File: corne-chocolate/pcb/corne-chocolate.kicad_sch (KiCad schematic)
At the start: 59 parts, among them J1 MJ-4PP-9, J2 OLED, P1 i2c-pin, P2 i2c-pin, SW1 SW_PUSH, SW10 SW_PUSH, SW11 SW_PUSH, SW12 SW_PUSH, SW13 SW_PUSH, SW14 SW_PUSH, SW15 SW_PUSH, SW16 SW_PUSH, SW17 SW_PUSH, SW18 SW_PUSH, SW19 SW_PUSH, SW2 SW_PUSH, SW20 SW_PUSH, SW21 SW_PUSH, SW3 SW_PUSH, SW4 SW_PUSH, SW5 SW_PUSH, SW6 SW_PUSH, SW7 SW_PUSH, SW8 SW_PUSH, SW9 SW_PUSH, U1 ProMicro

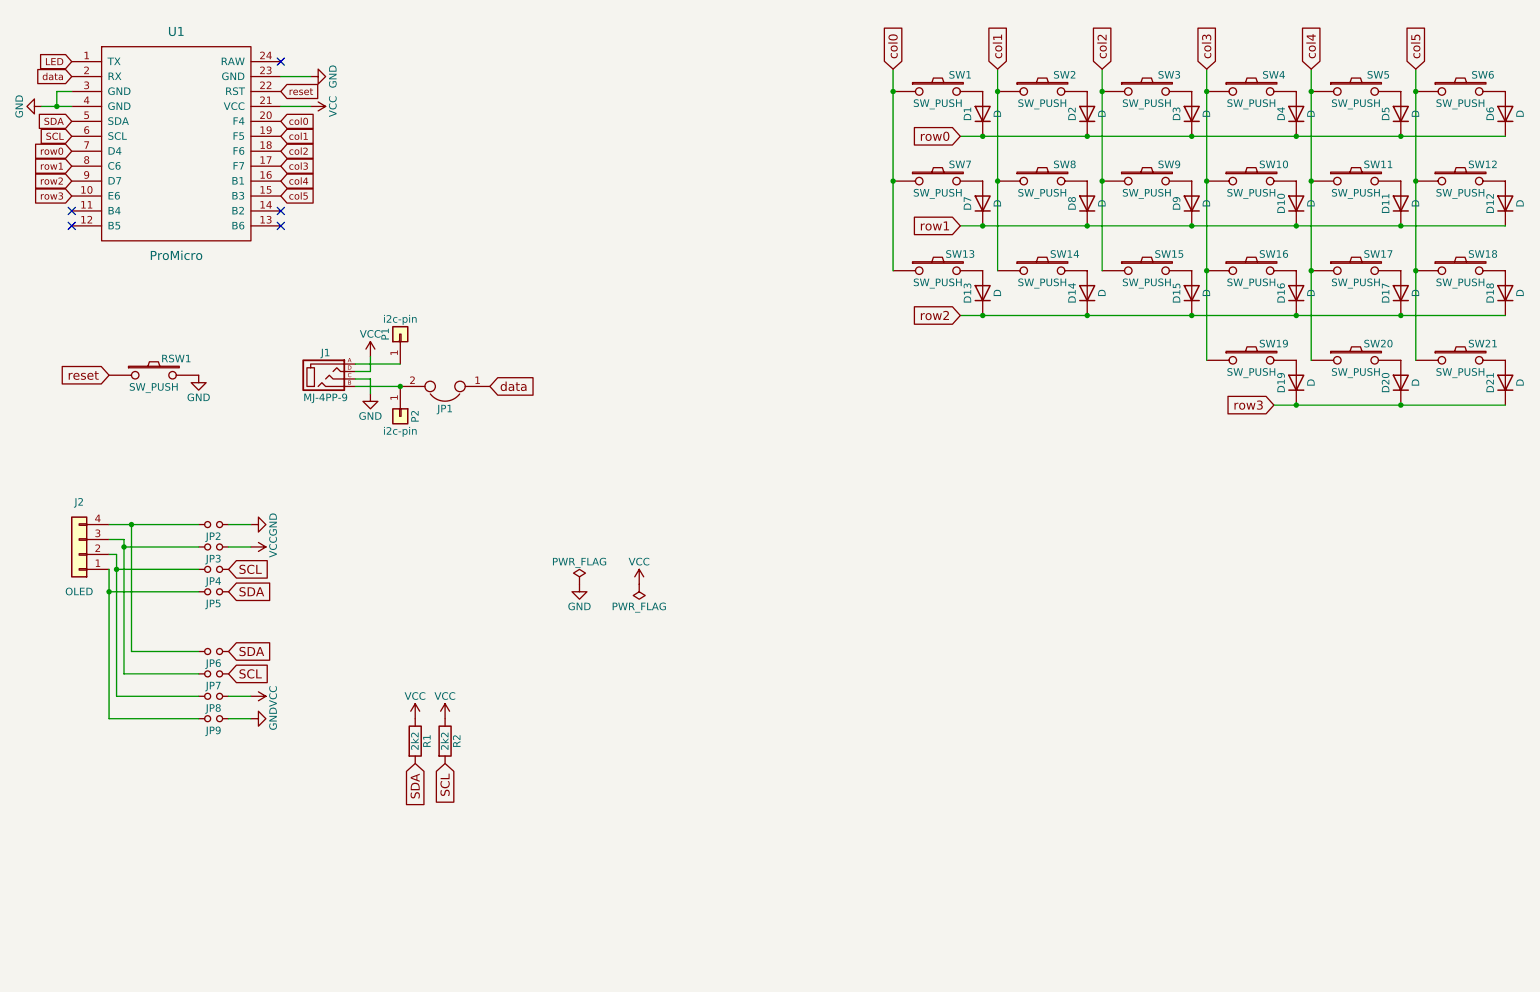
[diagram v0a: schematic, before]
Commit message: worked on schematic for handwired corne
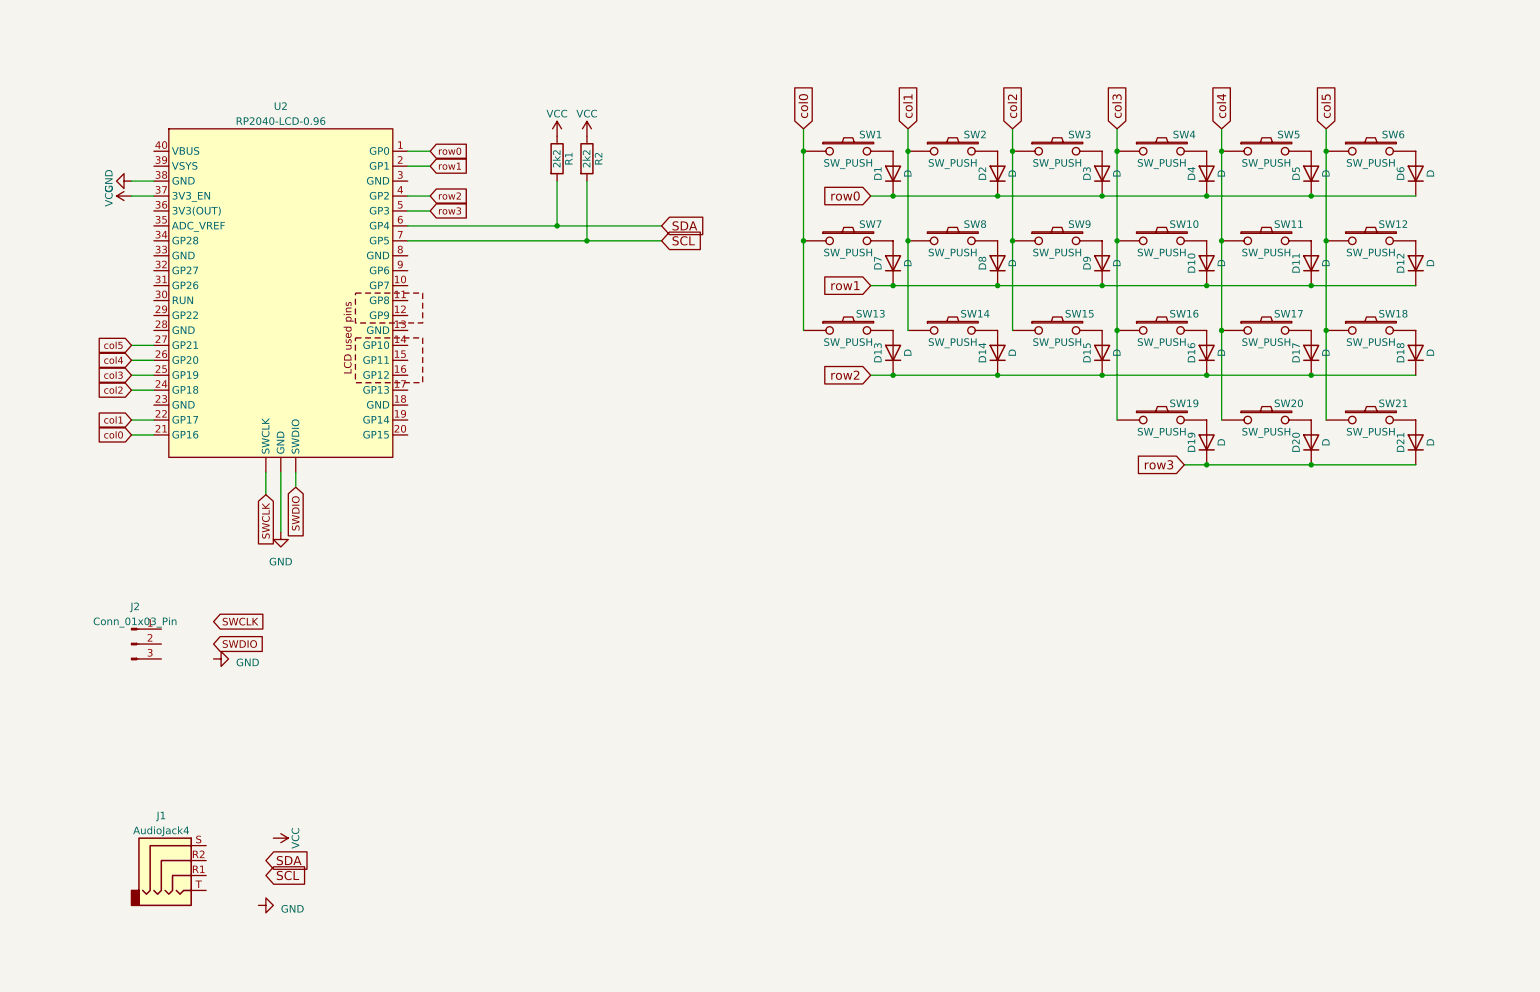
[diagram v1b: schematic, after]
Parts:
- removed J1: MJ-4PP-9, kbd:MJ-4PP-9, symbol corne-chocolate-rescue:MJ-4PP-9-kbd
- removed J2: OLED, kbd:OLED, symbol Connector_Generic:Conn_01x04
- removed JP1: (no value), kbd:JPC2, symbol corne-chocolate-rescue:Jumper-Device
- removed JP2, JP3, JP4, JP5, JP6, JP7, JP8, JP9: (no value), kbd:Jumper, symbol corne-chocolate-rescue:Jumper_NO_Small-Device
- removed P1, P2: i2c-pin, kbd:1pin_conn, symbol Connector_Generic:Conn_01x01
- removed RSW1: SW_PUSH, kbd:ResetSW, symbol corne-chocolate-rescue:SW_PUSH-kbd
- removed U1: ProMicro, kbd:ProMicro_v2, symbol corne-chocolate-rescue:ProMicro-kbd
- added J1: AudioJack4, symbol Connector_Audio:AudioJack4
- added J2: Conn_01x03_Pin, symbol Connector:Conn_01x03_Pin
- added U2: RP2040-LCD-0.96, symbol New_Library:Waveshare_RP2040-LCD-0.96
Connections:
- net GND: now also U2. (SWDIO), U2.38 (GND)
- net SCL: now also U2.7 (GP5)
- net SDA: now also U2.6 (GP4)
- net VCC: now also U2.37 (3V3_EN)
- net col0: now also U2.21 (GP16)
- net col1: now also U2.22 (GP17)
- net col2: now also U2.24 (GP18)
- net col3: now also U2.25 (GP19)
- net col4: now also U2.26 (GP20)
- net col5: now also U2.27 (GP21)
- net row0: now also U2.1 (GP0)
- net row1: now also U2.2 (GP1)
- net row2: now also U2.4 (GP2)
- net row3: now also U2.5 (GP3)
- new net SWCLK: U2. (SWDIO)
- new net SWDIO: U2. (SWDIO)
- no-connect marks 5 -> 0
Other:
- company: foostan -> SteScheller
- title: Corne Chocolate -> Handwired Corne
- moved on the sheet: D1, D10, D11, D12, D13, D14, D15, D16, D17, D18, D19, D2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

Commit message: finished schematic for keyboard
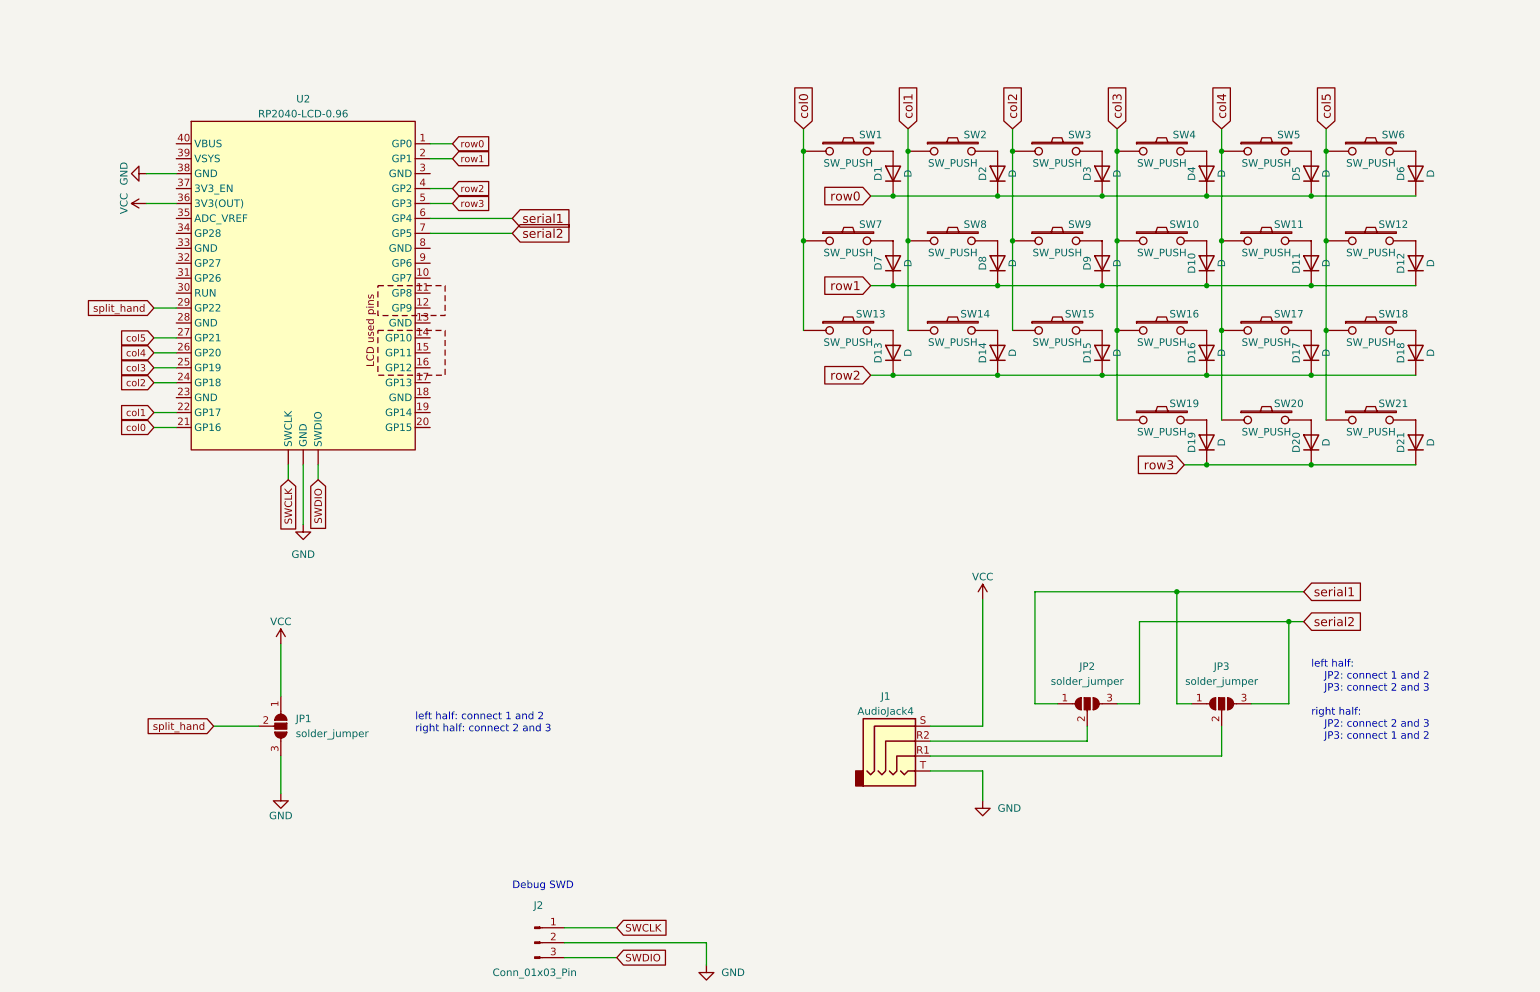
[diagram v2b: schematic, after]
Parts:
- removed R1, R2: 2k2, kbd:R, symbol Device:R
- added JP1, JP2, JP3: solder_jumper, symbol Jumper:SolderJumper_3_Open
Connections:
- net GND: now also J1.T, J2.2 (Pin_2), JP1.3 (B)
- net SWCLK: now also J2.1 (Pin_1)
- net SWDIO: now also J2.3 (Pin_3)
- net VCC: now also J1.S, U2.36 (3V3(OUT)), JP1.1 (A); no longer U2.37 (3V3_EN)
- net split_hand: now reaches U2.29 (GP22)
- net split_hand: now also JP1.2 (C)
- net at J1.R1: now also JP3.2 (C)
- net at J1.R2: now also JP2.2 (C)
- net SCL renamed serial2
- net serial2: now also JP2.3 (B), JP3.3 (B)
- net SDA renamed serial1
- net serial1: now also JP2.1 (A), JP3.1 (A)
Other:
- note added: "Debug SWD"
- note added: "left half: JP2: connect 1 and 2 JP3: connect 2 and 3 right half: JP2: connect 2 and 3 JP3: connect 1 and 2"
- note added: "left half: connect 1 and 2 right half: connect 2 and 3"
- moved on the sheet: J1, J2, U2
